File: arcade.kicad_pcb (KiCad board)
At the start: 2 copper layers, 55.3 x 42.7 mm, 37 parts, among them J1 VGA, J6 Term, Q1 BC847, Q2 BC847, U1 74LS86, U2 THS7375

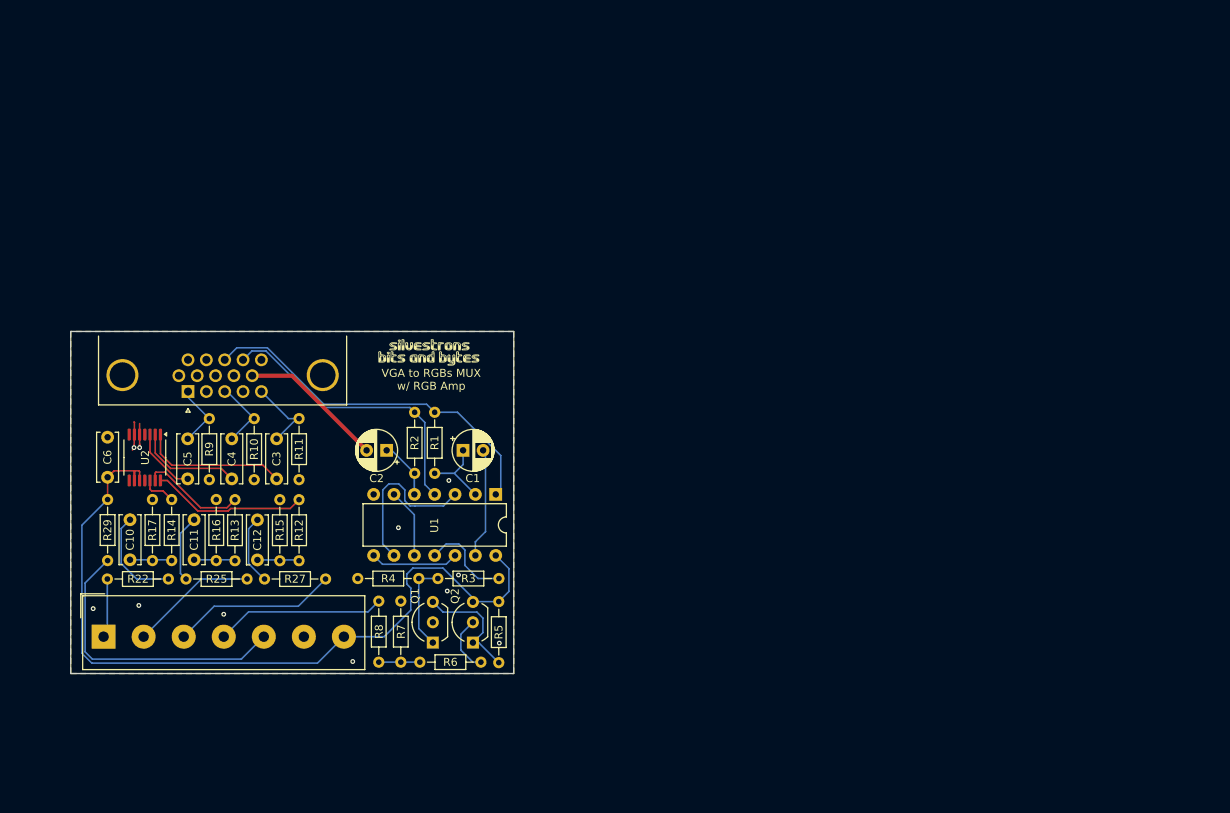
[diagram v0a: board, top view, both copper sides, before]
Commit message: second design for nec tv and with inputs integrated
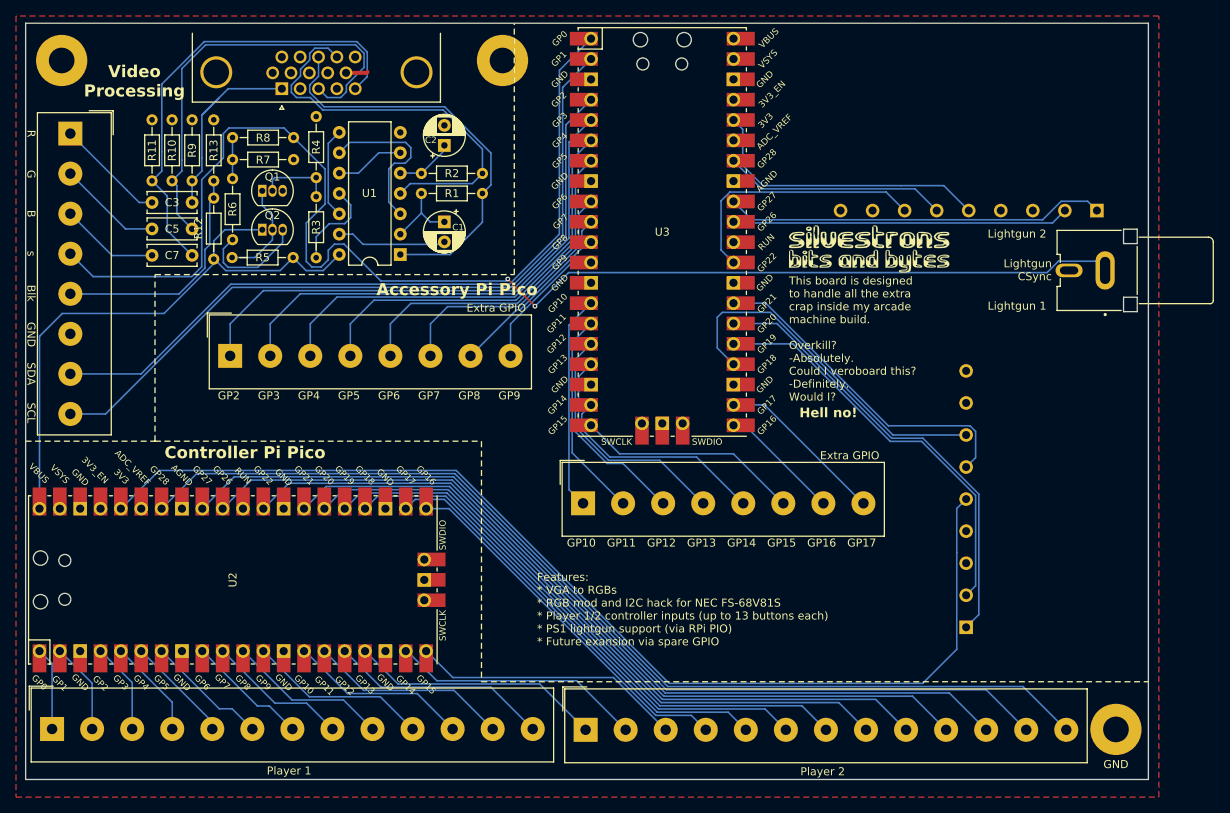
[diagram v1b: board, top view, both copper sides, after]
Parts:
- removed C10, C11, C12, C4, C6: 100n, Capacitor_THT:C_Disc_D6.0mm_W2.5mm_P5.00mm
- removed the G*** at (124.8, 86.0)
- removed R14, R15, R16, R17: 75, Resistor_THT:R_Axial_DIN0204_L3.6mm_D1.6mm_P7.62mm_Horizontal
- removed R22, R25, R27: 830, Resistor_THT:R_Axial_DIN0204_L3.6mm_D1.6mm_P7.62mm_Horizontal
- removed R29: 1k0, Resistor_THT:R_Axial_DIN0204_L3.6mm_D1.6mm_P7.62mm_Horizontal
- added C7: 100n, Capacitor_THT:C_Disc_D6.0mm_W2.5mm_P5.00mm, F.Cu at (95.5, 73.8)
- added G***: LOGO, KiCad Components:sbab-logo-20x6mm, F.Cu at (180.1, 73.0)
- added H1: MountingHole_Pad, MountingHole:MountingHole_3.2mm_M3_Pad, F.Cu at (79.3, 49.5)
- added H2: MountingHole_Pad, MountingHole:MountingHole_3.2mm_M3_Pad, F.Cu at (210.9, 133.0)
- added H2: MountingHole_Pad, MountingHole:MountingHole_3.2mm_M3_Pad, F.Cu at (134.3, 49.5)
- added J2: TV Interface, TerminalBlock_Altech:Altech_AK100_1x08_P5.00mm, F.Cu at (80.3, 58.6)
- added J3: Player 1, TerminalBlock_Altech:Altech_AK100_1x13_P5.00mm, F.Cu at (78.1, 132.9)
- added J4: Player 2, TerminalBlock_Altech:Altech_AK100_1x13_P5.00mm, F.Cu at (144.7, 133.0)
- added J5: Extra GPIO, TerminalBlock_Altech:Altech_AK100_1x08_P5.00mm, F.Cu at (100.3, 86.3)
- added J7: Lightgun 1, KiCad Components:PSX_Pad_Connector, F.Cu at (206.2, 104.2)
- added J8: Lightgun 2, KiCad Components:PSX_Pad_Connector, F.Cu at (192.5, 54.2)
- added J9: Lightgun Csync, KiCad Components:CUI_RCJ-047, F.Cu at (213.5, 75.7)
- added U3: Accessory Pico, KiCad Components:RPi_Pico_SMD_TH, F.Cu at (154.2, 70.9)
- J6: value Term -> Extra GPIO; footprint TerminalBlock_Altech:Altech_AK100_1x07_P5.00mm -> TerminalBlock_Altech:Altech_AK100_1x08_P5.00mm
- Q1, Q2: value BC847 -> BC547; footprint Package_TO_SOT_THT:TO-92_Inline_Wide -> Package_TO_SOT_THT:TO-92_Inline
- R12, R13: value 75 -> 1k0
- U2: value THS7375 -> Controller Pico; footprint Package_SO:TSSOP-14_4.4x5mm_P0.65mm -> KiCad Components:RPi_Pico_SMD_TH
- moved R7 66.2 mm to (100.6, 61.8), turned to 0 degrees
- moved J6 62.1 mm to (144.3, 104.8)
- moved R6 61.2 mm to (100.6, 71.8), turned to 90 degrees
- moved Q1 60.3 mm to (104.3, 65.7), turned to 0 degrees
- moved R8 58.8 mm to (108.2, 59.1), turned to 180 degrees
- moved Q2 57.9 mm to (104.3, 70.6), turned to 0 degrees
- moved R4 51.7 mm to (111.0, 64.1), turned to 90 degrees
- moved R5 50.0 mm to (108.2, 74.1), turned to 180 degrees
- moved R13 47.5 mm to (98.2, 64.5)
- moved R3 46.1 mm to (111.0, 74.1), turned to 90 degrees
- moved J1 39.6 mm to (106.8, 53.0)
- moved R12 39.1 mm to (98.2, 74.3)
- moved C2 38.7 mm to (127.0, 60.1), turned to 90 degrees
- moved R11 34.9 mm to (90.5, 64.5), turned to 90 degrees
- moved U1 32.2 mm to (121.5, 73.7), turned to 180 degrees
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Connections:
- C3 pad 1: IN B -> /Video Processing/IN R
- C3 pad 2: Net-(U2-CH1_IN) -> /Video Processing/RIN2
- C5 pad 1: IN R -> /Video Processing/IN G
- C5 pad 2: Net-(U2-CH3_IN) -> /Video Processing/GIN2
- J1 pad 1: IN R -> /Video Processing/IN R
- J1 pad 3: IN G -> /Video Processing/IN G
- J1 pad 5: IN B -> /Video Processing/IN B
- J6 pad 1: /rgb mod/OUT R -> /IO/GPIO34
- J6 pad 2: /rgb mod/OUT G -> /IO/GPIO35
- J6 pad 3: /rgb mod/OUT B -> /IO/GPIO36
- J6 pad 4: IN S -> /IO/GPIO37
- J6 pad 5: /rgb mod/OUT BLK -> /IO/GPIO38
- J6 pad 6: GND -> /IO/GPIO39
- J6 pad 7: 5V -> /IO/GPIO40
- Q1 pad 1: Net-(Q1-B) -> Net-(Q1-C)
- Q1 pad 2: GND -> Net-(Q1-B)
- Q1 pad 3: Net-(Q1-C) -> GND
- Q2 pad 1: Net-(Q1-C) -> +5V
- Q2 pad 2: Net-(Q2-E) -> Net-(Q1-C)
- Q2 pad 3: 5V -> Net-(Q2-E)
- R10 pad 1: IN G -> /Video Processing/IN G
- R11 pad 1: IN B -> /Video Processing/IN B
- R12 pad 1: AMP B -> +5V
- R12 pad 2: Net-(U2-CH1_OUT) -> /Video Processing/FBLIN2
- R13 pad 1: AMP G -> /Video Processing/FBLIN2
- R13 pad 2: Net-(U2-CH2_OUT) -> GND
- R5 pad 1: 5V -> +5V
- R8 pad 1: IN S -> /Video Processing/AV1-1
- R9 pad 1: IN R -> /Video Processing/IN R
- U1 pad 14: 5V -> +5V
- U2 pad 1: Net-(U2-CH1_IN) -> /IO/GPIO0
- U2 pad 10: 5V -> /IO/GPIO7
- U2 pad 11: unconnected-(U2-CH4_OUT-Pad11) -> /IO/GPIO8
- U2 pad 12: Net-(U2-CH3_OUT) -> /IO/GPIO9
- U2 pad 13: Net-(U2-CH2_OUT) -> GND
- U2 pad 14: Net-(U2-CH1_OUT) -> /IO/GPIO10
- U2 pad 2: Net-(U2-CH2_IN) -> /IO/GPIO1
- U2 pad 3: Net-(U2-CH3_IN) -> GND
- U2 pad 4: unconnected-(U2-CH4_IN-Pad4) -> /IO/GPIO2
- U2 pad 5: GND -> /IO/GPIO3
- U2 pad 6: GND -> /IO/GPIO4
- U2 pad 7: unconnected-(U2-NC-Pad7) -> /IO/GPIO5
- U2 pad 8: unconnected-(U2-NC-Pad8) -> GND
- U2 pad 9: 5V -> /IO/GPIO6
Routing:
- net /Video Processing/AV1-1: track 0.00 -> 171.1 mm, vias 0 -> 2
- net +3.3VP: track 0.00 -> 138.3 mm
- net /IO/GPIO25: track 0.00 -> 128.0 mm
- net /IO/GPIO24: track 0.00 -> 117.5 mm
- net /IO/GPIO23: track 0.00 -> 109.7 mm
- net 5V: track 100.9 -> 0.00 mm
- net /IO/GPIO22: track 0.00 -> 99.3 mm
- net /IO/SDA: track 0.00 -> 94.3 mm
- net /IO/SCL: track 0.00 -> 94.2 mm
- net /IO/GPIO21: track 0.00 -> 88.9 mm
- net /IO/GPIO20: track 0.00 -> 81.0 mm
- net +5V: track 0.00 -> 74.9 mm
- net /IO/GPIO19: track 0.00 -> 73.1 mm
- net /IO/GPIO26: track 0.00 -> 68.8 mm
- net /IO/GPIO18: track 0.00 -> 65.2 mm
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- removed copper zone on B.Cu, net GND
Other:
- board size 55.3 x 42.7 mm -> 140.1 x 94.4 mm
- board text added: "Accessory Pi Pico"
- board text added: "B"
- board text added: "Blk"
- board text added: "Controller Pi Pico"
- board text added: "Extra GPIO"
- board text added: "Features: * VGA to RGBs * RGB mod and I2C hack for NEC FS-68V81S * Player 1/2 controller inputs (up to 13 buttons each) * PS1 lightgun support (via RPi PIO) * Future exansion via spare GPIO"
- board text added: "G"
- board text added: "GND"
- board text added: "GP10"
- board text added: "GP11"
- board text added: "GP12"
- board text added: "GP13"
- board text added: "GP14"
- board text added: "GP15"
- board text added: "GP16"
- board text added: "GP17"
- board text added: "GP2"
- board text added: "GP3"
- board text added: "GP4"
- board text added: "GP5"
- board text added: "GP6"
- board text added: "GP7"
- board text added: "GP8"
- board text added: "GP9"
- board text added: "Hell no!"
- board text added: "Lightgun 1"
- board text added: "Lightgun 2"
- board text added: "Lightgun CSync"
- board text added: "Player 1"
- board text added: "Player 2"
- board text added: "R"
- board text added: "SCL"
- board text added: "SDA"
- board text added: "This board is designed to handle all the extra crap inside my arcade machine build. Overkill? -Absolutely. Could I veroboard this? -Definitely. Would I?"
- board text added: "Video Processing"
- board text added: "s"
- board text removed: "VGA to RGBs MUX w/ RGB Amp"
